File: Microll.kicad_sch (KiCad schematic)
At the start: 40 parts, among them J1 Conn_01x12, J2 Conn_02x10_Top_Bottom, J3 Conn_01x08, J6 USB_C_Receptacle_USB2.0_16P, SW4 SW_DIP_x03, U1 ESP32-C3-WROOM-02-N4, U2 TLV76733DRVx, U3 STM32G0B1CBT6, U4 BSD235NH6327XTSA1, U5 DPDT_Switch_x2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

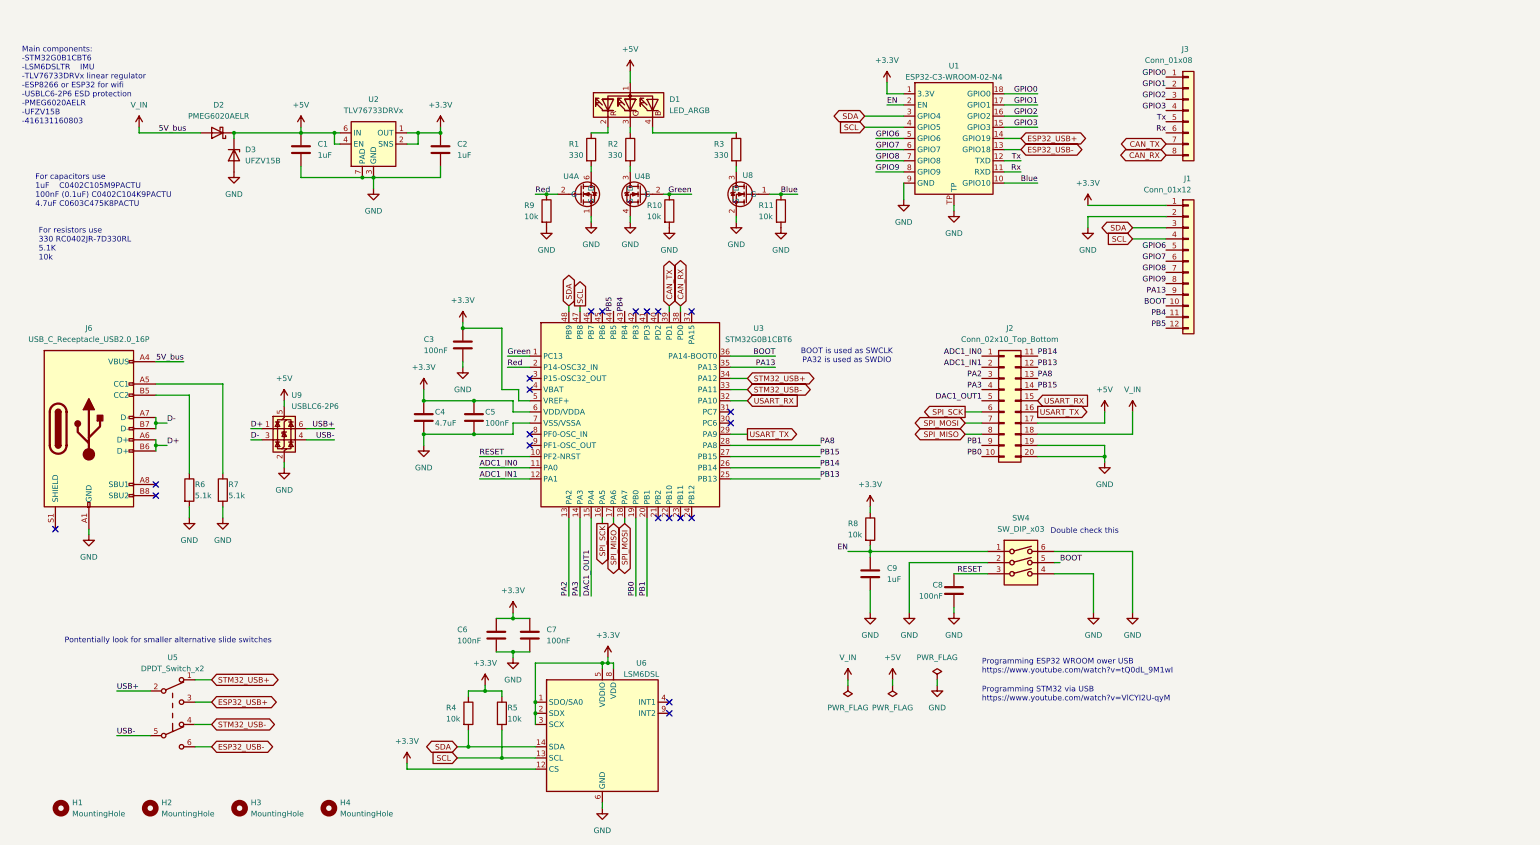
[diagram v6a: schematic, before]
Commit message: Added datasheets to components. Ready to proceed with layout update
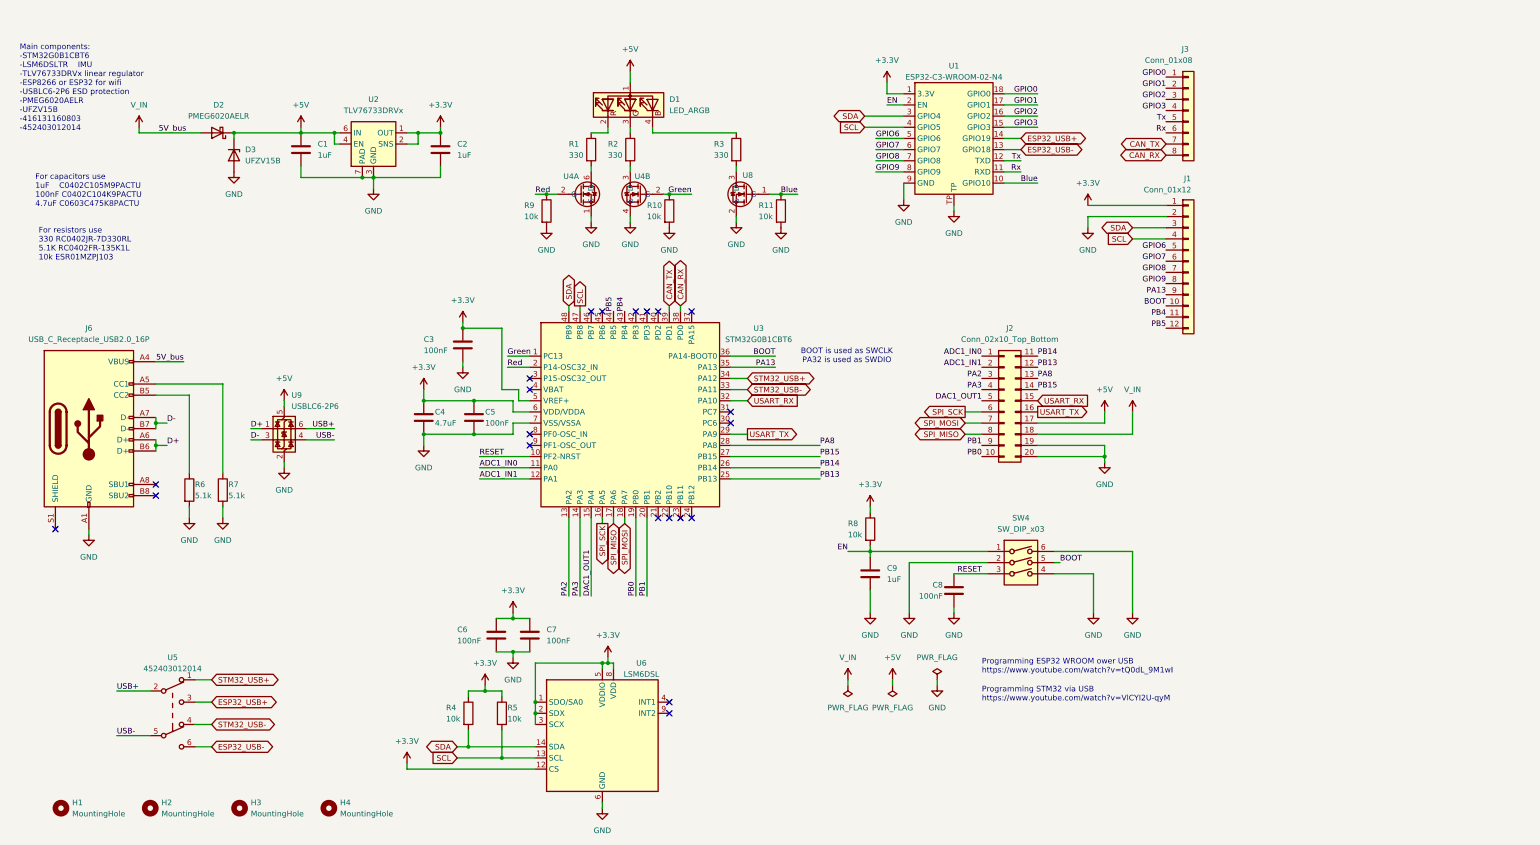
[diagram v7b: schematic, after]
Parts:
- U5: value DPDT_Switch_x2 -> 452403012014
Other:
- note added: "For capacitors use 1uF C0402C105M9PACTU 100nF C0402C104K9PACTU 4.7uF C0603C475K8PACTU"
- note added: "For resistors use 330 RC0402JR-7D330RL 5.1K RC0402FR-135K1L 10k ESR01MZPJ103"
- note added: "Main components: -STM32G0B1CBT6 -LSM6DSLTR IMU -TLV76733DRVx linear regulator -ESP8266 or ESP32 for wifi -USBLC6-2P6 ESD protection -PMEG6020AELR -UFZV15B -416131160803 -452403012014"
- note removed: "Double check this"
- note removed: "For capacitors use 1uF C0402C105M9PACTU 100nF (0.1uF) C0402C104K9PACTU 4.7uF C0603C475K8PACTU"
- note removed: "For resistors use 330 RC0402JR-7D330RL 5.1K 10k"
- note removed: "Main components: -STM32G0B1CBT6 -LSM6DSLTR IMU -TLV76733DRVx linear regulator -ESP8266 or ESP32 for wifi -USBLC6-2P6 ESD protection -PMEG6020AELR -UFZV15B -416131160803"
- note removed: "Pontentially look for smaller alternative slide switches"
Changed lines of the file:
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@@
 		)
 	)
-	(text "For capacitors use\n1uF	C0402C105M9PACTU\n100nF (0.1uF) C0402C104K9PACTU\n4.7uF C0603C475K8PACTU"
+	(text "For capacitors use\n1uF	C0402C105M9PACTU\n100nF C0402C104K9PACTU\n4.7uF C0603C475K8PACTU"
 		(exclude_from_sim no)
 		(at 15.748 50.038 0)
@@
 		)
 	)
-	(text "Main components:\n-STM32G0B1CBT6	\n-LSM6DSLTR	IMU\n-TLV76733DRVx linear regulator\n-ESP8266 or ESP32 for wifi\n-USBLC6-2P6 ESD protection\n-PMEG6020AELR\n-UFZV15B\n-416131160803\n"
+	(text "Main components:\n-STM32G0B1CBT6	\n-LSM6DSLTR	IMU\n-TLV76733DRVx linear regulator\n-ESP8266 or ESP32 for wifi\n-USBLC6-2P6 ESD protection\n-PMEG6020AELR\n-UFZV15B\n-416131160803\n-452403012014\n"
 		(exclude_from_sim no)
-		(at 12.7 31.242 0)
+		(at 12.192 32.766 0)
 		(effects
 			(font
@@
 		)
 	)
-	(text "Double check this"
-		(exclude_from_sim no)
-		(at 254.508 123.698 0)
-		(effects
-			(font
-				(size 1.27 1.27)
-			)
-		)
-	)
-	(text "For resistors use\n330 RC0402JR-7D330RL\n5.1K\n10k"
+	(text "For resistors use\n330 RC0402JR-7D330RL\n5.1K RC0402FR-135K1L\n10k ESR01MZPJ103"
 		(exclude_from_sim no)
 		(at 16.51 62.23 0)
@@
 		)
 	)
-	(text "Pontentially look for smaller alternative slide switches"
-		(exclude_from_sim no)
-		(at 45.974 148.59 0)
-		(effects
-			(font
-				(size 1.27 1.27)
-			)
-		)
-	)
 	(label "EN"
 		(at 200.66 128.27 180)
@@
 			)
 		)
-		(property "Datasheet" "~"
+		(property "Datasheet" "https://fscdn.rohm.com/en/products/databook/datasheet/passive/resistor/chip_resistor/esr-e.pdf"
 			(at 185.42 50.8 0)
 			(effects
@@
 			)
 		)
-		(property "Datasheet" "~"
+		(property "Datasheet" "https://ksim3.kemet.com/capacitor-simulation?pn=C0402C104K9PACTU&disty=mouser"
 			(at 113.03 81.28 0)
 			(effects
@@
 			)
 		)
-		(property "Datasheet" "~"
+		(property "Datasheet" "https://eu.mouser.com/datasheet/2/447/KEM_C1006_X5R_SMD-3316465.pdf"
 			(at 76.2 36.83 0)
 			(effects
@@
 			)
 		)
-		(property "Datasheet" "~"
+		(property "Datasheet" "https://fscdn.rohm.com/en/products/databook/datasheet/passive/resistor/chip_resistor/esr-e.pdf"
 			(at 160.02 50.8 0)
 			(effects
@@
 			)
 		)
-		(property "Datasheet" "~"
+		(property "Datasheet" "https://ksim3.kemet.com/capacitor-simulation?pn=C0603C475K8PACTU&disty=mouser"
 			(at 104.14 97.79 0)
 			(effects
@@
 			)
 		)
-		(property "Datasheet" "~"
+		(property "Datasheet" "https://fscdn.rohm.com/en/products/databook/datasheet/passive/resistor/chip_resistor/esr-e.pdf"
 			(at 132.08 50.8 0)
 			(effects
@@
 			)
 		)
-		(property "Datasheet" "~"
+		(property "Datasheet" "https://fscdn.rohm.com/en/products/databook/datasheet/passive/resistor/chip_resistor/esr-e.pdf"
 			(at 114.3 165.1 0)
 			(effects
@@
 			)
 		)
-		(property "Datasheet" "~"
+		(property "Datasheet" "https://ksim3.kemet.com/capacitor-simulation?pn=C0402C104K9PACTU&disty=mouser"
 			(at 224.79 137.16 0)
 			(effects
@@
 			)
 		)
-		(property "Datasheet" "~"
+		(property "Datasheet" "https://fscdn.rohm.com/en/products/databook/datasheet/passive/resistor/chip_resistor/esr-e.pdf"
 			(at 121.92 165.1 0)
 			(effects
@@
 			)
 		)
-		(property "Datasheet" "~"
+		(property "Datasheet" "https://eu.mouser.com/datasheet/2/447/KEM_C1006_X5R_SMD-3316465.pdf"
 			(at 205.74 133.35 0)
 			(effects
@@
 			)
 		)
-		(property "Datasheet" "~"
+		(property "Datasheet" "https://eu.mouser.com/datasheet/2/447/KEM_C1006_X5R_SMD-3316465.pdf"
 			(at 107.95 36.83 0)
 			(effects
@@
 			)
 		)
-		(property "Datasheet" "~"
+		(property "Datasheet" "https://www.farnell.com/datasheets/2550265.pdf"
 			(at 278.13 62.23 0)
 			(effects
@@
 			)
 		)
-		(property "Description" "Generic connector, single row, 01x12, script generated (kicad-library-utils/schlib/autogen/connector/)"
+		(property "Description" "SAMTEC SSW-112-01-G-S"
 			(at 278.13 62.23 0)
 			(effects
@@
 			)
 		)
-		(property "Datasheet" "~"
+		(property "Datasheet" "https://www.farnell.com/datasheets/2550265.pdf"
 			(at 236.22 93.98 0)
 			(effects
@@
 			)
 		)
-		(property "Description" "Generic connector, double row, 02x10, top/bottom pin numbering scheme (row 1: 1...pins_per_row, row2: pins_per_row+1 ... num_pins), script generated (kicad-library-utils/schlib/autogen/connector/)"
+		(property "Description" "SAMTEC SSW-110-01-G-D"
 			(at 236.22 93.98 0)
 			(effects
@@
 			)
 		)
-		(property "Datasheet" "~"
+		(property "Datasheet" "https://www.farnell.com/datasheets/2550265.pdf"
 			(at 278.13 27.94 0)
 			(effects
@@
 			)
 		)
-		(property "Description" "Generic connector, single row, 01x08, script generated (kicad-library-utils/schlib/autogen/connector/)"
+		(property "Description" "SAMTEC SSW-108-01-G-S"
 			(at 278.13 27.94 0)
 			(effects
@@
 			)
 		)
-		(property "Datasheet" "~"
+		(property "Datasheet" "https://www.mouser.co.uk/datasheet/2/447/PYu_RC_Group_51_RoHS_L_12-3368608.pdf"
 			(at 50.8 114.3 0)
 			(effects
@@
 			)
 		)
-		(property "Datasheet" "~"
+		(property "Datasheet" "https://ksim3.kemet.com/capacitor-simulation?pn=C0402C104K9PACTU&disty=mouser"
 			(at 128.27 147.32 0)
 			(effects
@@
 			)
 		)
-		(property "Datasheet" "~"
+		(property "Datasheet" "https://www.mouser.co.uk/datasheet/2/447/PYu_RC_Group_51_RoHS_L_12-3368608.pdf"
 			(at 58.42 114.3 0)
 			(effects
@@
 			)
 		)
-		(property "Value" "DPDT_Switch_x2"
+		(property "Value" "452403012014"
 			(at 46.99 154.94 0)
 			(effects
@@
 			)
 		)
-		(property "Description" ""
+		(property "Description" "SPST slide switch"
 			(at 46.99 165.1 0)
 			(effects
@@
 			)
 		)
-		(property "Datasheet" "~"
+		(property "Datasheet" "https://ksim3.kemet.com/capacitor-simulation?pn=C0402C104K9PACTU&disty=mouser"
 			(at 120.65 147.32 0)
 			(effects
@@
 			)
 		)
-		(property "Datasheet" "~"
+		(property "Datasheet" "https://fscdn.rohm.com/en/products/databook/datasheet/passive/resistor/chip_resistor/esr-e.pdf"
 			(at 205.74 123.19 0)
 			(effects
@@
 			)
 		)
-		(property "Datasheet" "~"
+		(property "Datasheet" "https://www.we-online.com/components/products/datasheet/416131160803.pdf"
 			(at 240.03 133.35 0)
 			(effects
@@
 			)
 		)
-		(property "Description" "3x DIP Switch, Single Pole Single Throw (SPST) switch, small symbol"
+		(property "Description" "416131160803"
 			(at 240.03 130.81 0)
 			(effects

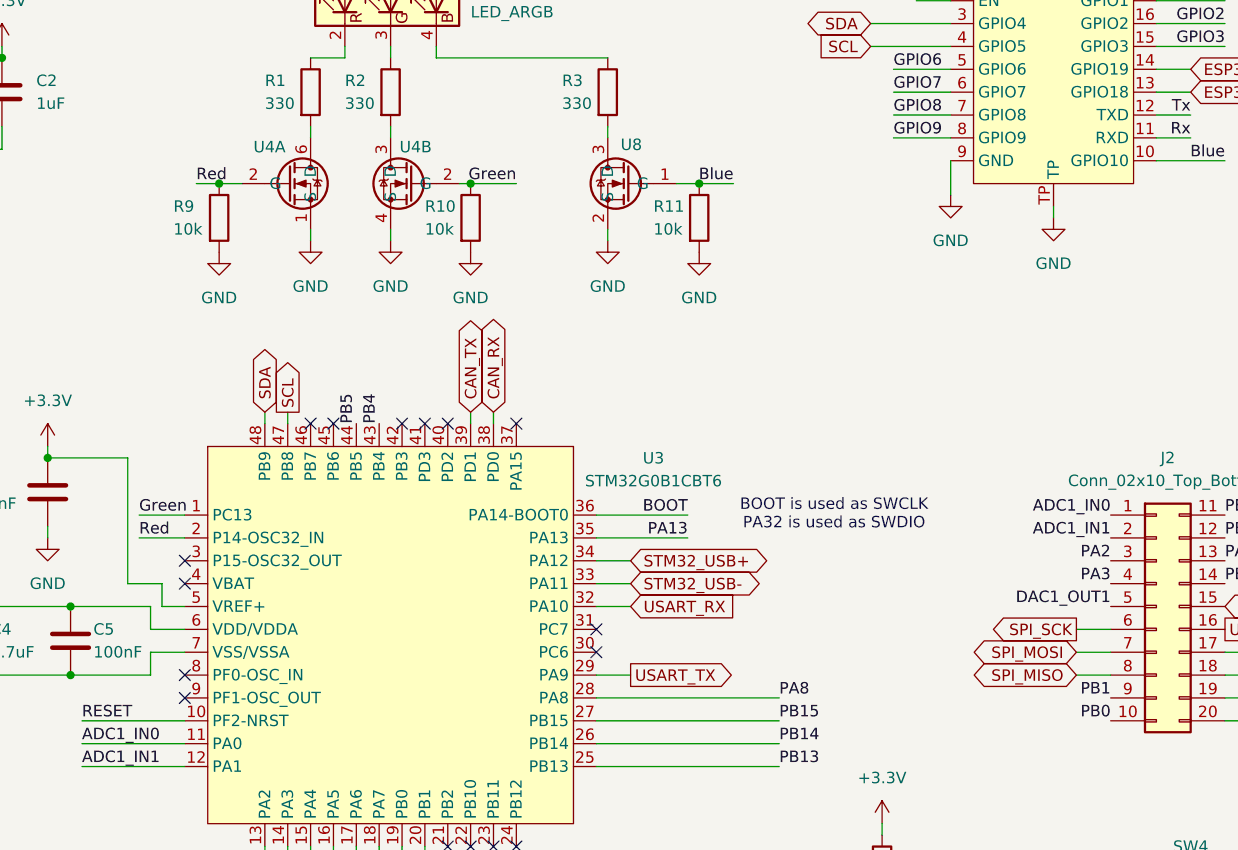
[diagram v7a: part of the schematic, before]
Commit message: Updated PCB to Microll V3
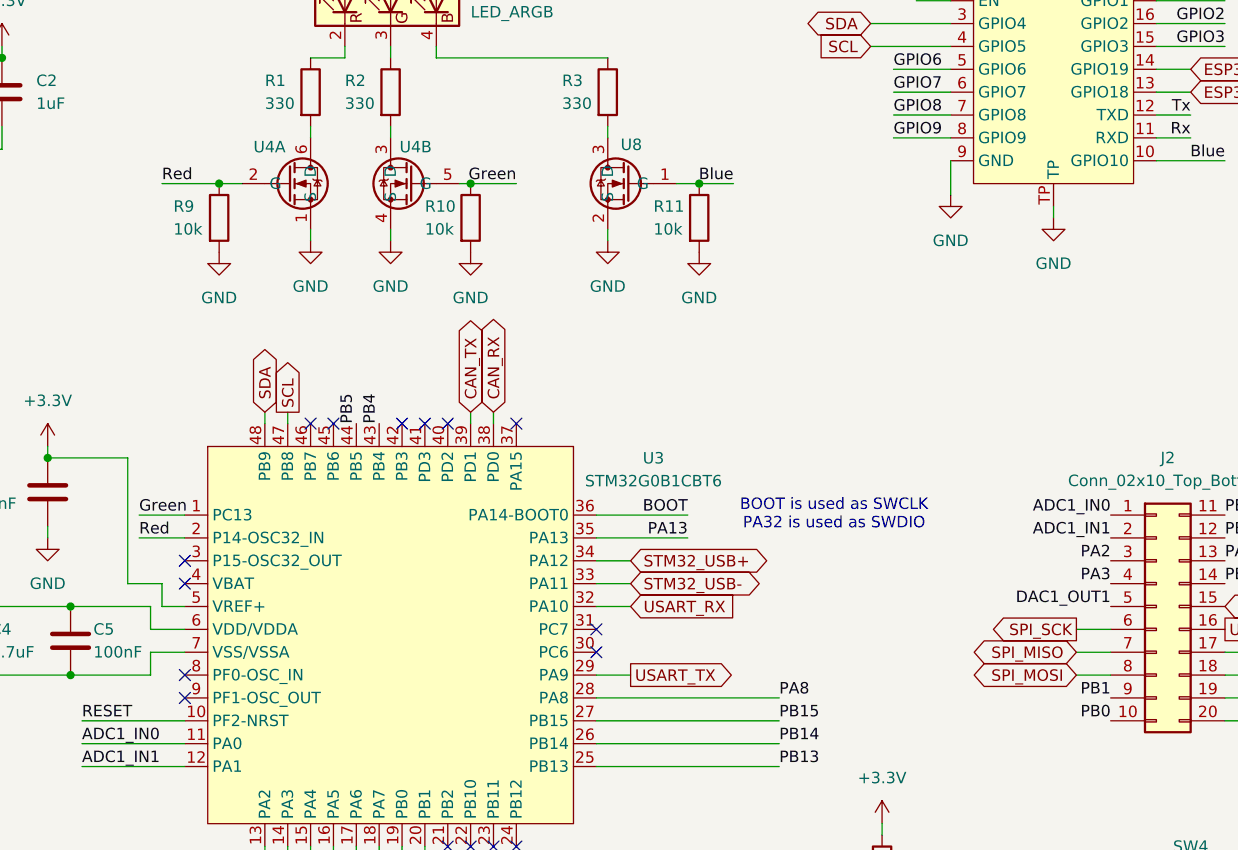
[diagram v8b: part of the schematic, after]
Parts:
- SW4: footprint Button_Switch_SMD:SW_DIP_SPSTx03_Slide_KingTek_DSHP03TJ_W5.25mm_P1.27mm_JPin -> 416131160803:WE_DIP_SWITCH_3_POS
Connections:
- net Green: now also U4.5 (G); no longer U4.2 (G)
- net SPI_MISO: now also J2.7 (Pin_7); no longer J2.8 (Pin_8)
- net SPI_MOSI: now also J2.8 (Pin_8); no longer J2.7 (Pin_7)
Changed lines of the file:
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@@
 	(wire
 		(pts
-			(xy 132.08 46.99) (xy 134.62 46.99)
+			(xy 243.84 26.67) (xy 236.22 26.67)
 		)
 		(stroke
@@
 	(wire
 		(pts
-			(xy 243.84 26.67) (xy 236.22 26.67)
+			(xy 142.24 120.65) (xy 142.24 138.43)
 		)
 		(stroke
@@
 	(wire
 		(pts
-			(xy 142.24 120.65) (xy 142.24 138.43)
+			(xy 194.31 109.22) (xy 173.99 109.22)
 		)
 		(stroke
@@
 	(wire
 		(pts
-			(xy 194.31 109.22) (xy 173.99 109.22)
+			(xy 77.47 102.87) (xy 83.82 102.87)
 		)
 		(stroke
@@
 	(wire
 		(pts
-			(xy 77.47 102.87) (xy 83.82 102.87)
+			(xy 125.73 46.99) (xy 132.08 46.99)
 		)
 		(stroke
@@
 	(wire
 		(pts
-			(xy 129.54 46.99) (xy 132.08 46.99)
+			(xy 114.3 172.72) (xy 129.54 172.72)
 		)
 		(stroke
@@
 	(wire
 		(pts
-			(xy 114.3 172.72) (xy 129.54 172.72)
+			(xy 265.43 128.27) (xy 265.43 142.24)
 		)
 		(stroke
@@
 	(wire
 		(pts
-			(xy 265.43 128.27) (xy 265.43 142.24)
+			(xy 175.26 40.64) (xy 175.26 41.91)
 		)
 		(stroke
@@
 	(wire
 		(pts
-			(xy 175.26 40.64) (xy 175.26 41.91)
+			(xy 236.22 24.13) (xy 243.84 24.13)
 		)
 		(stroke
@@
 	(wire
 		(pts
-			(xy 236.22 24.13) (xy 243.84 24.13)
+			(xy 132.08 46.99) (xy 134.62 46.99)
 		)
 		(stroke
@@
 	)
 	(label "Red"
-		(at 129.54 46.99 0)
+		(at 125.73 46.99 0)
 		(fields_autoplaced yes)
 		(effects
@@
 	(global_label "SPI_MISO"
 		(shape bidirectional)
-		(at 227.33 101.6 180)
+		(at 227.33 99.06 180)
 		(fields_autoplaced yes)
 		(effects
@@
 		)
 		(property "Intersheetrefs" "${INTERSHEET_REFS}"
-			(at 214.5854 101.6 0)
+			(at 214.5854 99.06 0)
 			(effects
 				(font
@@
 	(global_label "SPI_MOSI"
 		(shape bidirectional)
-		(at 227.33 99.06 180)
+		(at 227.33 101.6 180)
 		(fields_autoplaced yes)
 		(effects
@@
 		)
 		(property "Intersheetrefs" "${INTERSHEET_REFS}"
-			(at 214.5854 99.06 0)
+			(at 214.5854 101.6 0)
 			(effects
 				(font
@@
 	)
 	(symbol
+		(lib_name "BSD235NH6327XTSA1_1")
 		(lib_id "BSD235NH6327XTSA1:BSD235NH6327XTSA1")
 		(at 142.24 46.99 0)
@@
 		(pin "1"
 		)
-		(pin "2"
+		(pin "5"
 		)
 		(instances
@@
 		(pin "1"
 		)
-		(pin "2"
+		(pin "5"
 		)
 		(instances
@@
 			)
 		)
-		(property "Footprint" "Button_Switch_SMD:SW_DIP_SPSTx03_Slide_KingTek_DSHP03TJ_W5.25mm_P1.27mm_JPin"
+		(property "Footprint" "416131160803:WE_DIP_SWITCH_3_POS"
 			(at 240.03 133.35 0)
 			(effects
